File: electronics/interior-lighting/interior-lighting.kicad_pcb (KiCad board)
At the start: 2 copper layers, 45 x 45 mm, 48 parts, among them U1 APA102-2020, U10 APA102-2020, U11 APA102-2020, U12 APA102-2020, U13 APA102-2020, U14 APA102-2020, U15 APA102-2020, U16 APA102-2020, U17 APA102-2020, U18 APA102-2020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

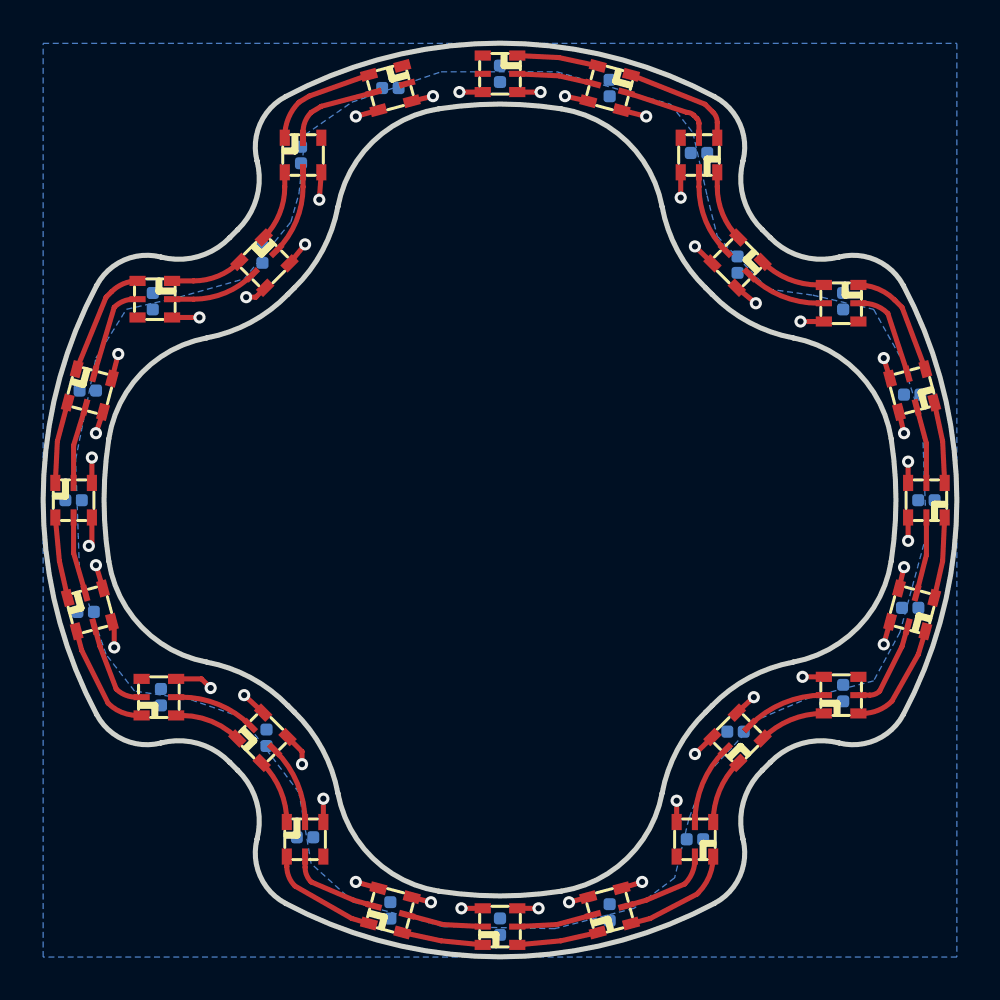
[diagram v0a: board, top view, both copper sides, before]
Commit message: Internal lighting board finished
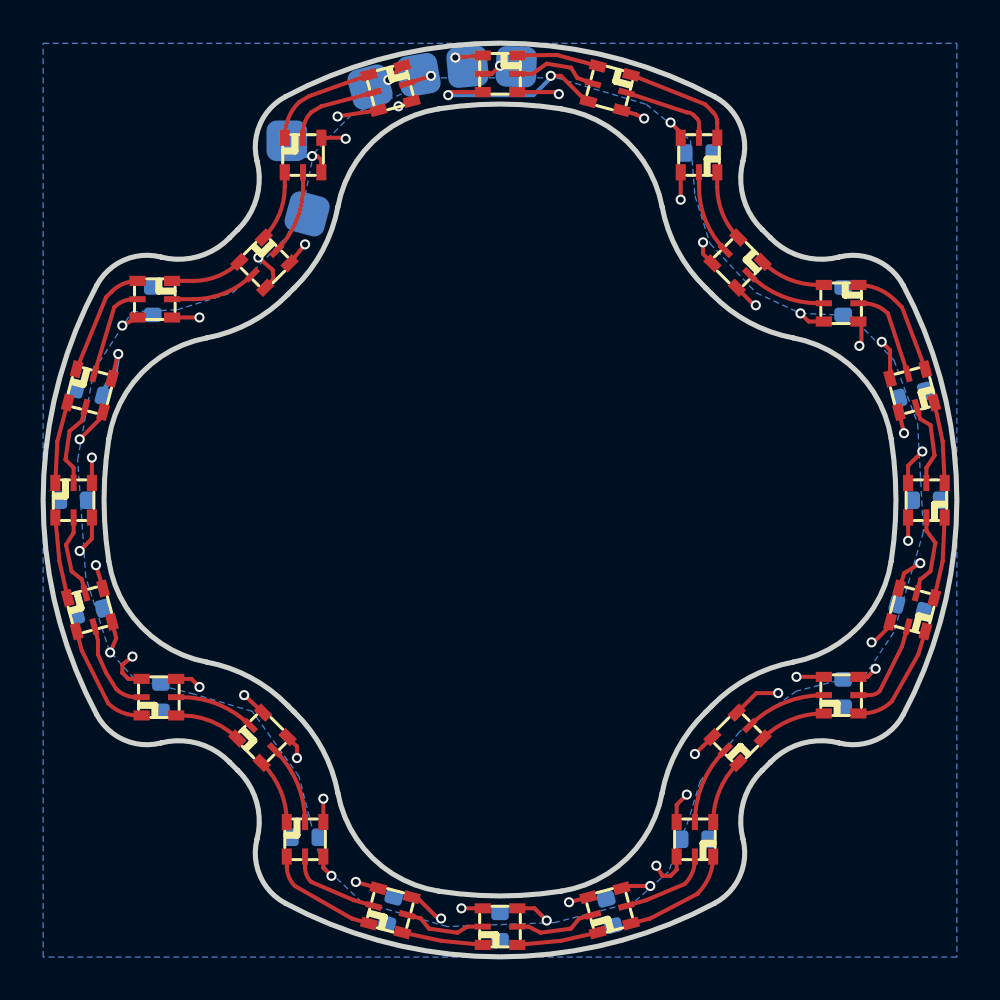
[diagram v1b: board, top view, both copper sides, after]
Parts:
- removed C1, C10, C16, C2, C22, C23, C24, C4: 100n_X7R_1005M, Applidyne_Capacitor:CAPC1005X60N
- added P1: PAD_SOLDER_2mm, Applidyne_Connector:PAD_SOLDER_2mm_SQUARE, B.Cu at (89.5, 82.3)
- added P2: PAD_SOLDER_2mm, Applidyne_Connector:PAD_SOLDER_2mm_SQUARE, B.Cu at (100.8, 78.7)
- added P3: PAD_SOLDER_2mm, Applidyne_Connector:PAD_SOLDER_2mm_SQUARE, B.Cu at (98.4, 78.7)
- added P4: PAD_SOLDER_2mm, Applidyne_Connector:PAD_SOLDER_2mm_SQUARE, B.Cu at (90.5, 85.9)
- added P5: PAD_SOLDER_2mm, Applidyne_Connector:PAD_SOLDER_2mm_SQUARE, B.Cu at (93.6, 79.7)
- added P6: PAD_SOLDER_2mm, Applidyne_Connector:PAD_SOLDER_2mm_SQUARE, B.Cu at (96.0, 79.0)
- C11, C12, C13, C14, C15, C17, C18, C19, C20, C21, C3, C5, C6, C7, C8, C9: value 100n_X7R_1005M -> 100n_X7R_1608M; footprint Applidyne_Capacitor:CAPC1005X60N -> Applidyne_Capacitor:CAPC1608X90L
- moved C18 0.20 mm to (79.8, 105.5), turned to -165 degrees
- moved C20 0.14 mm to (79.8, 94.7), turned to 165 degrees
- turned C12 to -75 degrees
- turned C14 to -105 degrees
- turned C6 to 15 degrees
- turned C8 to -15 degrees
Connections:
- U1 pad 2: unconnected-(U1-SDI-Pad2) -> Net-(P3-P1)
- U1 pad 3: unconnected-(U1-CKI-Pad3) -> Net-(P2-P1)
- U24 pad 1: unconnected-(U24-SDO-Pad1) -> Net-(P5-P1)
- U24 pad 6: unconnected-(U24-CK0-Pad6) -> Net-(P6-P1)
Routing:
- net GND: track 24.2 -> 45.3 mm, vias 20 -> 24
- net +3.3V: track 23.4 -> 33.4 mm, vias 20 -> 24
- net Net-(P5-P1): track 0.00 -> 1.92 mm, vias 0 -> 1
- net Net-(P6-P1): track 0.00 -> 1.87 mm, vias 0 -> 1
- net Net-(P3-P1): track 0.00 -> 1.35 mm, vias 0 -> 1
- net Net-(P2-P1): track 0.00 -> 1.02 mm, vias 0 -> 1
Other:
- board text added: "+"
- board text added: "-"
- board text added: "2 layer 1.6mm FR4 low-cost board 1oz copper weight HASL surface finish Black Soldermask White or No Silkscreen"
- board text added: "C"
- board text added: "D"
- board text added: "MANUFACTURING NOTES"
- board text added: "S.RAPSON"
- board text added: "V1.0"
